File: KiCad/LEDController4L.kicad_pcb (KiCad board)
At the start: 4 copper layers, 50 x 50 mm, 40 parts, among them J1 Conn_01x05, J2 UART, J3 JTAG, J5 USB_C_Receptacle_USB2.0_16P, J6 Conn_01x03, J7 VDD, J8 GND, J9 Conn_01x14, Q1 IRLZ44N, Q2 IRLZ44N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

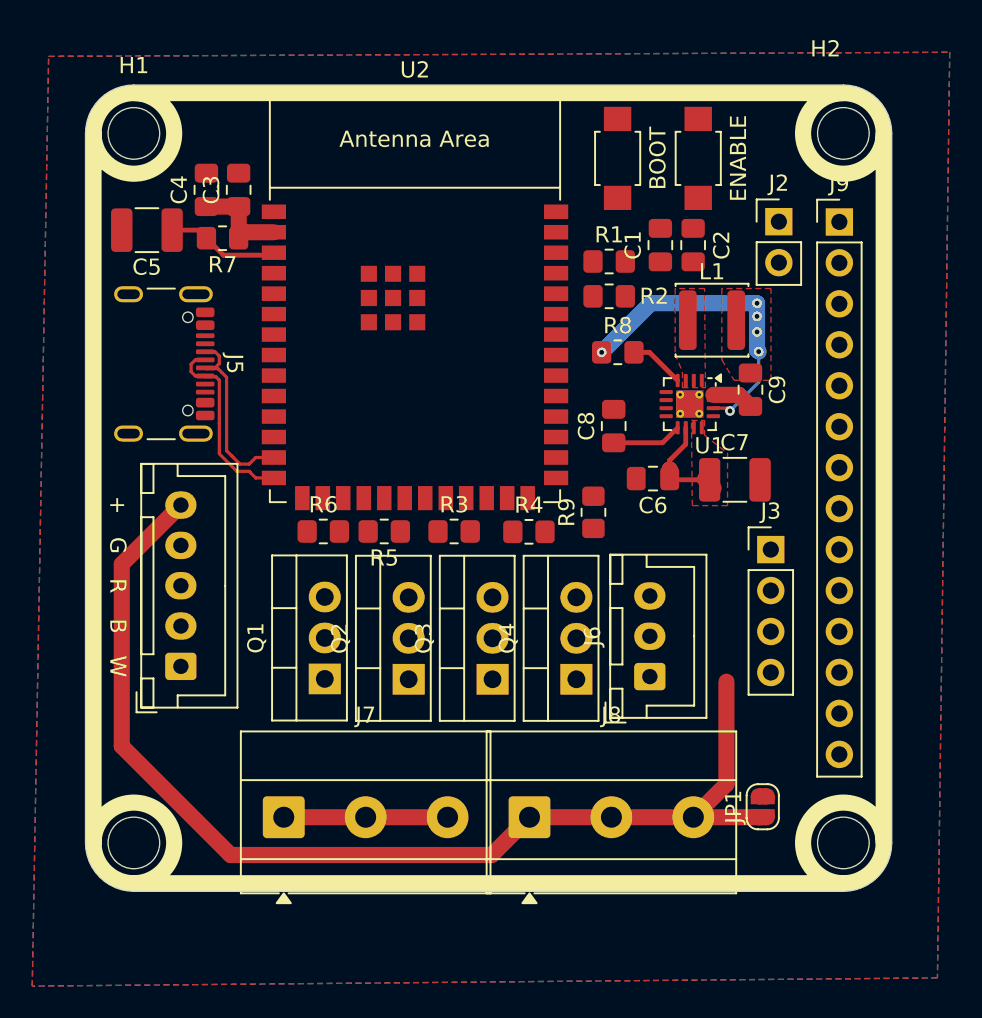
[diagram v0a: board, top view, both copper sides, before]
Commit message: convert to 4 layer pcb
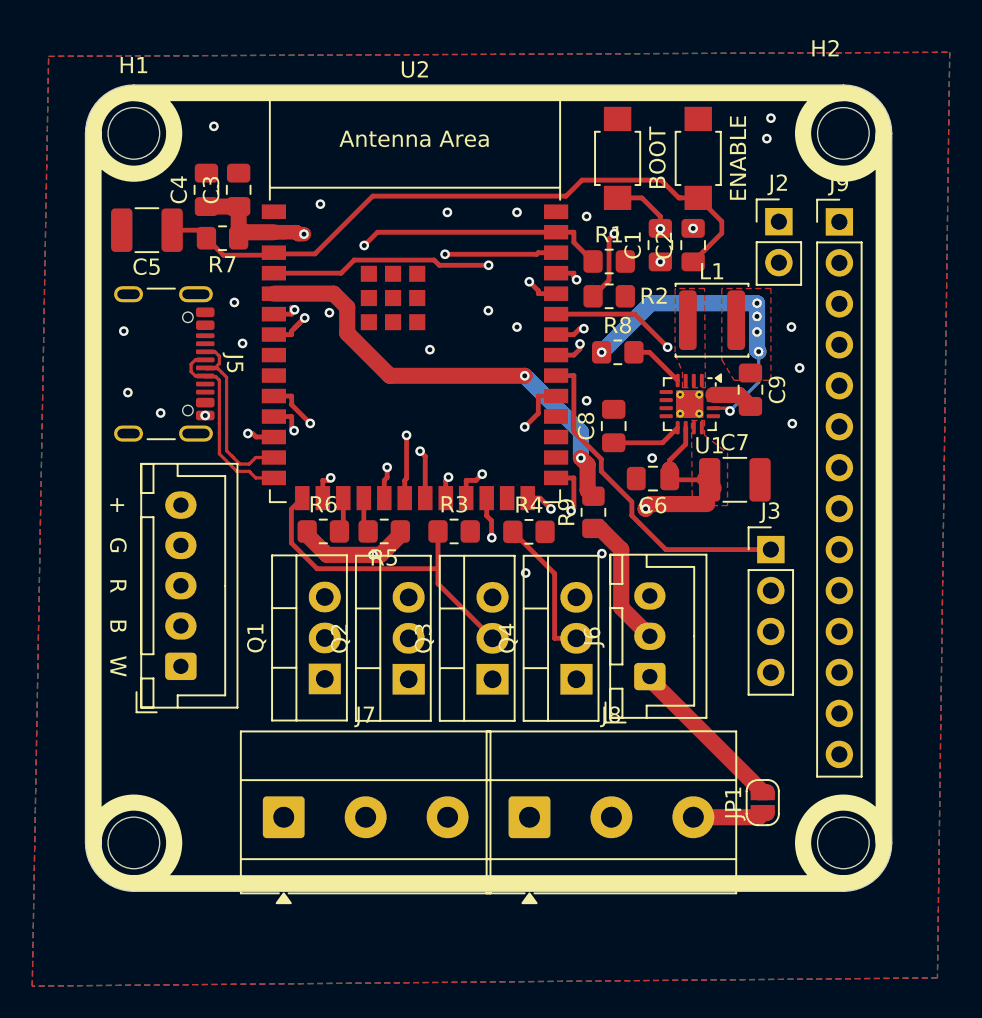
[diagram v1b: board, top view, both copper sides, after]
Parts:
- moved JP1 0.26 mm to (127.0, 93.5)
- turned C2 to -90 degrees
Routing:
- net W: track 0.00 -> 48.2 mm, vias 0 -> 1
- net G: track 0.00 -> 47.9 mm, vias 0 -> 2
- net +3.3V: track 25.8 -> 73.3 mm, vias 6 -> 10
- net GPIO.11: track 0.00 -> 46.4 mm, vias 0 -> 1
- net GPIO.8: track 0.00 -> 42.0 mm, vias 0 -> 1
- net GPIO.7: track 0.00 -> 41.1 mm, vias 0 -> 1
- net R: track 0.00 -> 41.0 mm, vias 0 -> 1
- net GPIO.46: track 0.00 -> 40.1 mm, vias 0 -> 1
- net GPIO.6: track 0.00 -> 39.3 mm, vias 0 -> 1
- net GPIO.18: track 0.00 -> 38.9 mm, vias 0 -> 1
- net GPIO.17: track 0.00 -> 38.3 mm, vias 0 -> 1
- net GPIO.38: track 0.00 -> 34.1 mm, vias 0 -> 2
- net ESP_EN: track 7.02 -> 41.1 mm
- net GPIO.21: track 0.00 -> 32.4 mm, vias 0 -> 1
- net GPIO.12: track 0.00 -> 32.4 mm, vias 0 -> 1
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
